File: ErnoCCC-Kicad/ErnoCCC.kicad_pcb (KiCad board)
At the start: 2 copper layers, 161.4 x 95.9 mm, 96 parts, among them J1 6VAC, J2 ICSP, J3 FTDI, J4 Erno Controller, J5 SWITCH, J6 LED OUT, J7 Conn_01x05, Q1 BC847, Q2 BC847, SW1 SW_Push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

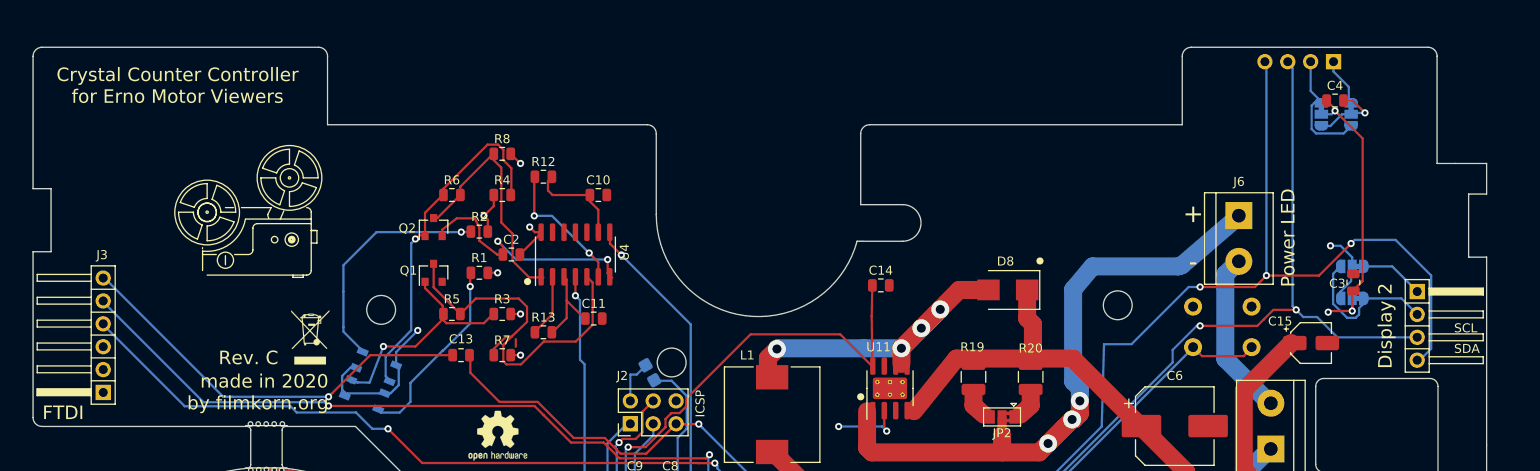
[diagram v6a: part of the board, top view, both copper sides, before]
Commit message: Fixed Exe Distance, fixed Display Position, fixed missing i2c on DAC, added Diode to Motor Out, Added labels to pinouts, removed Peephole LED
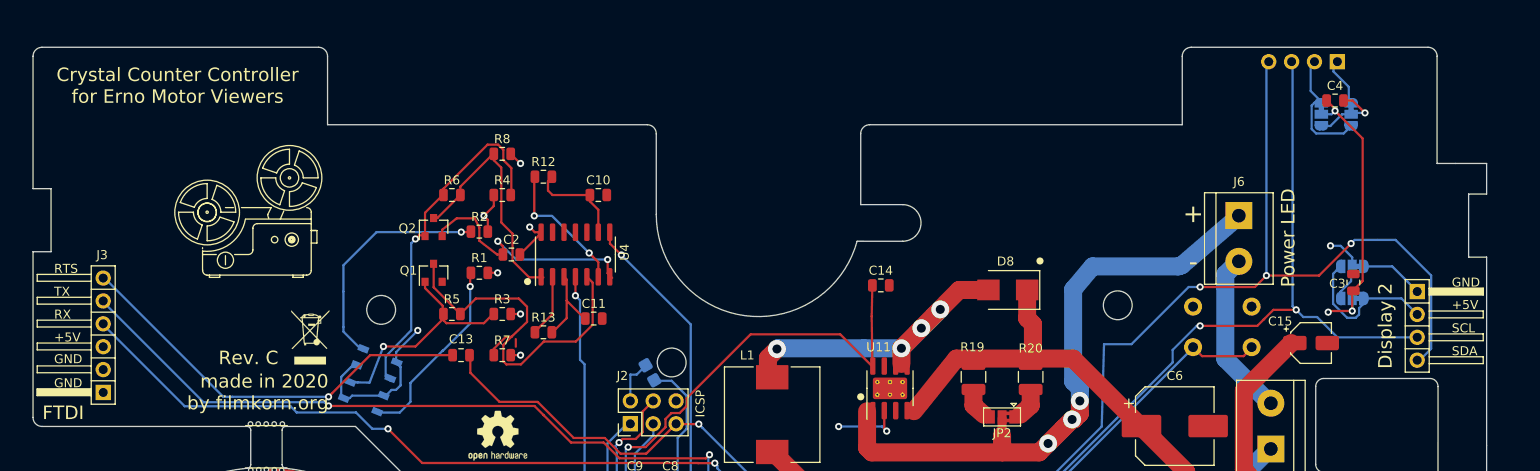
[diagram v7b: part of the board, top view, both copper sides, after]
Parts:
- moved D7 0.43 mm to (208.0, 26.8)
- moved U2 0.34 mm to (101.5, 60.1)
- moved U1 0.28 mm to (99.8, 64.3)
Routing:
- net GND: track 108.7 -> 109.3 mm
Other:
- board text added: "RTS"
- board text added: "RX"
- board text added: "TX"
- board text added: "VCC"
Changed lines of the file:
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@@
   (general
     (thickness 1.6)
-    (drawings 324)
-    (tracks 992)
+    (drawings 340)
+    (tracks 995)
     (zones 0)
     (modules 96)
@@
   )
   (module ErnoCCC:QRE1113GR-slim locked (layer B.Cu)
-    (at 99.931 64 158)
+    (at 99.822 64.262 158)
     (fp_text reference U1 (at -3.973563 0.044784 338) (layer B.SilkS)
       (effects (font (size 1 1) (thickness 0.15)) (justify mirror))
@@
   )
   (module ErnoCCC:QRE1113GR-slim locked (layer B.Cu)
-    (at 101.4 60.4 338)
+    (at 101.473 60.071 338)
     (fp_text reference U2 (at 4.116288 0.308473 338) (layer B.SilkS)
       (effects (font (size 1 1) (thickness 0.15)) (justify mirror))
@@
   )
   (module Connector_PinHeader_2.54mm:PinHeader_1x04_P2.54mm_Vertical (layer B.Cu)
-    (at 207.6 26.8 90)
+    (at 208.026 26.8 90)
     (descr "Through hole straight pin header, 1x04, 2.54mm pitch, single row")
     (tags "Through hole pin header THT 1x04 2.54mm single row")
-    (fp_text reference D7 (at 0 2.33 270) (layer B.SilkS)
+    (fp_text reference D7 (at 0 2.33) (layer B.SilkS)
       (effects (font (size 1 1) (thickness 0.15)) (justify mirror))
     )
@@
     )
   )
+  (gr_line (start 83.929 50.496) (end 83.929 50.75) (layer F.SilkS) (width 0.12))
+  (gr_line (start 83.929 50.75) (end 82.786 50.75) (layer F.SilkS) (width 0.12))
+  (gr_line (start 82.786 50.75) (end 82.786 50.496) (layer F.SilkS) (width 0.12))
+  (gr_arc (start 82.552666 49.982581) (end 82.037267 49.981782) (angle -84.13445268) (layer F.SilkS) (width 0.12))
+  (gr_text RTS (at 65.532 49.784) (layer F.SilkS)
+    (effects (font (size 1 1) (thickness 0.15)) (justify left))
+  )
+  (gr_text GND (at 65.532 59.817) (layer F.SilkS)
+    (effects (font (size 1 1) (thickness 0.15)) (justify left))
+  )
+  (gr_text +5V (at 65.532 57.404) (layer F.SilkS)
+    (effects (font (size 1 1) (thickness 0.15)) (justify left))
+  )
+  (gr_text GND (at 65.532 62.484) (layer F.SilkS)
+    (effects (font (size 1 1) (thickness 0.15)) (justify left))
+  )
+  (gr_text RX (at 65.532 54.864) (layer F.SilkS)
+    (effects (font (size 1 1) (thickness 0.15)) (justify left))
+  )
+  (gr_text TX (at 65.532 52.324) (layer F.SilkS)
+    (effects (font (size 1 1) (thickness 0.15)) (justify left))
+  )
+  (gr_text SDA (at 200.66 28.702) (layer B.SilkS)
+    (effects (font (size 1 1) (thickness 0.15)) (justify left mirror))
+  )
+  (gr_text SCL (at 203.962 28.702) (layer B.SilkS)
+    (effects (font (size 1 1) (thickness 0.15)) (justify left mirror))
+  )
+  (gr_text VCC (at 207.264 28.702) (layer B.SilkS)
+    (effects (font (size 1 1) (thickness 0.15)) (justify left mirror))
+  )
+  (gr_text GND (at 211.074 28.702) (layer B.SilkS)
+    (effects (font (size 1 1) (thickness 0.15)) (justify left mirror))
+  )
+  (gr_text GND (at 220.726 51.308) (layer F.SilkS)
+    (effects (font (size 1 1) (thickness 0.15)) (justify left))
+  )
+  (gr_text +5V (at 220.726 53.8) (layer F.SilkS)
+    (effects (font (size 1 1) (thickness 0.15)) (justify left))
+  )
   (gr_arc (start 218.1 26.2) (end 219.1 26.2) (angle -90) (layer Edge.Cuts) (width 0.05))
   (gr_arc (start 191.8 26.2) (end 191.8 25.2) (angle -90) (layer Edge.Cuts) (width 0.05))
@@
     (effects (font (size 2 2) (thickness 0.2)))
   )
-  (gr_text SCL (at 220.98 56.388) (layer F.SilkS)
+  (gr_text SCL (at 220.726 56.388) (layer F.SilkS)
     (effects (font (size 1 1) (thickness 0.15)) (justify left))
   )
-  (gr_text SDA (at 220.98 58.674) (layer F.SilkS)
+  (gr_text SDA (at 220.726 58.928) (layer F.SilkS)
     (effects (font (size 1 1) (thickness 0.15)) (justify left))
   )
@@
     (effects (font (size 1 1) (thickness 0.15)) (justify right))
   )
-  (gr_text "Cut/Shorten \nboth Jumpers \nto swap Display \npolarity" (at 204 33.1) (layer B.SilkS)
+  (gr_text "Cut/Shorten \nboth Jumpers \nto swap Display \npolarity" (at 203.962 34.29) (layer B.SilkS)
     (effects (font (size 1 1) (thickness 0.15)) (justify left mirror))
   )
@@
   (segment (start 142.494 101.581587) (end 142.494 102.108) (width 0.25) (layer F.Cu) (net 37))
   (segment (start 97.524441 61.689971) (end 98.508412 60.706) (width 0.25) (layer B.Cu) (net 37))
-  (segment (start 97.524441 63.226114) (end 97.524441 61.689971) (width 0.25) (layer B.Cu) (net 37))
-  (segment (start 97.816206 63.517879) (end 97.524441 63.226114) (width 0.25) (layer B.Cu) (net 37))
-  (segment (start 97.816206 63.895365) (end 97.816206 63.517879) (width 0.25) (layer B.Cu) (net 37))
   (segment (start 98.508412 60.706) (end 99.06 60.706) (width 0.25) (layer B.Cu) (net 37))
-  (segment (start 103.806559 62.710029) (end 103.806559 60.880559) (width 0.25) (layer B.Cu) (net 37))
-  (segment (start 102.906513 63.610075) (end 103.806559 62.710029) (width 0.25) (layer B.Cu) (net 37))
-  (segment (start 102.245609 63.610075) (end 102.906513 63.610075) (width 0.25) (layer B.Cu) (net 37))
-  (segment (start 103.806559 60.880559) (end 103.378 60.452) (width 0.25) (layer B.Cu) (net 37))
-  (segment (start 98.085066 63.626505) (end 101.981495 63.626505) (width 0.25) (layer B.Cu) (net 37))
-  (segment (start 97.816206 63.895365) (end 98.085066 63.626505) (width 0.25) (layer B.Cu) (net 37))
-  (segment (start 101.981495 63.626505) (end 102.108 63.5) (width 0.25) (layer B.Cu) (net 37))
   (via (at 105.918 56.642) (size 0.8) (drill 0.4) (layers F.Cu B.Cu) (net 37))
   (segment (start 103.514794 59.045206) (end 105.918 56.642) (width 0.25) (layer B.Cu) (net 37))
-  (segment (start 103.514794 60.504635) (end 103.514794 59.045206) (width 0.25) (layer B.Cu) (net 37))
   (segment (start 114.73115 48.21) (end 115.298 48.21) (width 0.25) (layer F.Cu) (net 37))
   (segment (start 112.758 46.686) (end 114.73115 48.21) (width 0.25) (layer F.Cu) (net 37))
@@
   (segment (start 209.677 48.53) (end 208.391 47.244) (width 0.25) (layer B.Cu) (net 37))
   (segment (start 209.677 49.53) (end 209.677 48.53) (width 0.25) (layer B.Cu) (net 37))
+  (segment (start 97.415441 61.798971) (end 97.415441 63.887441) (width 0.25) (layer B.Cu) (net 37))
+  (segment (start 97.524441 61.689971) (end 97.415441 61.798971) (width 0.25) (layer B.Cu) (net 37))
+  (segment (start 97.415441 63.887441) (end 97.536 64.008) (width 0.25) (layer B.Cu) (net 37))
+  (segment (start 97.536 64.008) (end 97.663 64.008) (width 0.25) (layer B.Cu) (net 37))
+  (segment (start 98.354327 64.157365) (end 98.630692 63.881) (width 0.25) (layer B.Cu) (net 37))
+  (segment (start 97.707206 64.157365) (end 98.354327 64.157365) (width 0.25) (layer B.Cu) (net 37))
+  (segment (start 102.379588 63.881) (end 103.014588 63.246) (width 0.25) (layer B.Cu) (net 37))
+  (segment (start 98.630692 63.881) (end 102.379588 63.881) (width 0.25) (layer B.Cu) (net 37))
+  (segment (start 103.014588 63.246) (end 103.505 63.246) (width 0.25) (layer B.Cu) (net 37))
+  (segment (start 103.505 63.246) (end 104.013 62.738) (width 0.25) (layer B.Cu) (net 37))
+  (segment (start 104.013 62.738) (end 104.013 60.706) (width 0.25) (layer B.Cu) (net 37))
+  (segment (start 104.013 60.706) (end 103.505 60.198) (width 0.25) (layer B.Cu) (net 37))
+  (segment (start 103.514794 59.045206) (end 103.514794 60.061206) (width 0.25) (layer B.Cu) (net 37))
+  (segment (start 103.514794 60.061206) (end 103.505 60.071) (width 0.25) (layer B.Cu) (net 37))
   (via (at 96.012 64.008) (size 0.8) (drill 0.4) (layers F.Cu B.Cu) (net 38))
   (segment (start 109.7885 59.386) (end 100.634 59.386) (width 0.25) (layer F.Cu) (net 38))

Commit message: Gute Nacht
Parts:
- D10: value Peephole -> D_Schottky_Small; footprint LED_SMD:LED_0805_2012Metric_Castellated -> Diode_SMD:D_SMB; moved to F.Cu
- moved REF** 48.8 mm to (161.6, 82.2)
- moved D10 18.2 mm to (114.8, 68.3), turned to 0 degrees
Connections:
- D10 pad 1: Net-(D10-Pad1) -> /VCTRL
- D10 pad 2: +5V -> Net-(D10-Pad2)
- D2 pad 1: Net-(D10-Pad1) -> +5V
- D3 pad 1: Net-(D10-Pad1) -> +5V
- D4 pad 1: Net-(D10-Pad1) -> +5V
- D5 pad 1: Net-(D10-Pad1) -> +5V
- D6 pad 1: Net-(D10-Pad1) -> +5V
- R14 pad 1: Net-(D10-Pad1) -> +5V
- U7 pad 4: Net-(U7-Pad4) -> /SDA
- U7 pad 5: Net-(U7-Pad5) -> /SCL
- U9 pad 5: /VCTRL -> Net-(D10-Pad2)
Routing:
- net Net-(D10-Pad1): track 85.2 -> 0.00 mm, vias 1 -> 0
- net +5V: track 122.5 -> 147.6 mm
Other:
- board text added: "+18V"
- board text removed: "+15V"
